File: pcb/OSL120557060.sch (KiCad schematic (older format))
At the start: 78 parts, among them J1 USB_B_Micro, J2 USB_B_Micro, J3 AVR-ISP-6, SW1 SW_SPST, SW10 SW_SPST, SW11 SW_SPST, SW12 SW_SPST, SW13 SW_SPST, SW14 SW_SPST, SW15 SW_SPST, SW16 SW_SPST, SW17 SW_SPST, SW18 SW_SPST, SW19 SW_SPST, SW2 SW_SPST, SW20 SW_SPST, SW21 SW_SPST, SW22 SW_SPST, SW23 SW_SPST, SW24 SW_SPST, SW25 SW_SPST, SW26 SW_SPST, SW27 SW_SPST, SW28 SW_SPST, SW29 SW_SPST, SW3 SW_SPST, SW30 SW_SPST, SW4 SW_SPST, SW5 SW_SPST, SW6 SW_SPST, SW7 SW_SPST, SW8 SW_SPST, SW9 SW_SPST, U1 ATmega328-PU, X1 16MHz

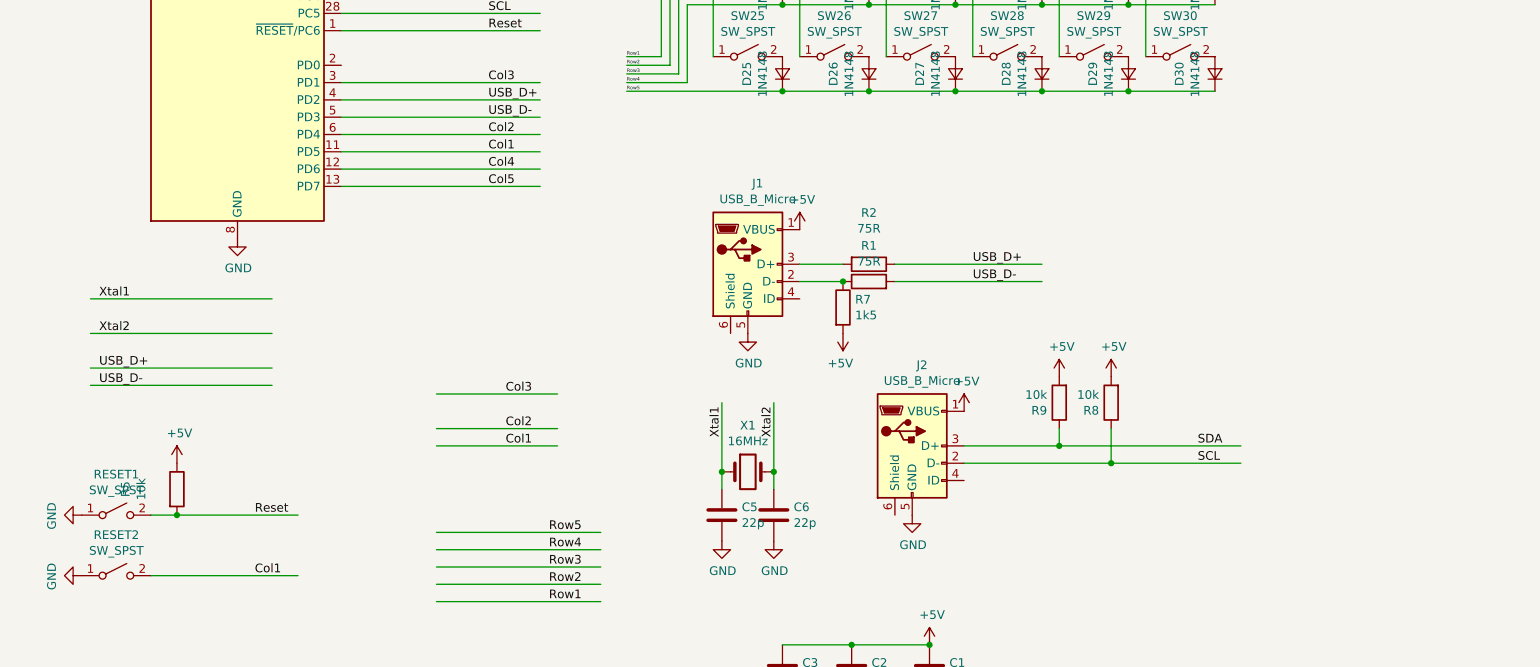
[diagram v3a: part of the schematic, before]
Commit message: * added missing zener diodes on the usb port
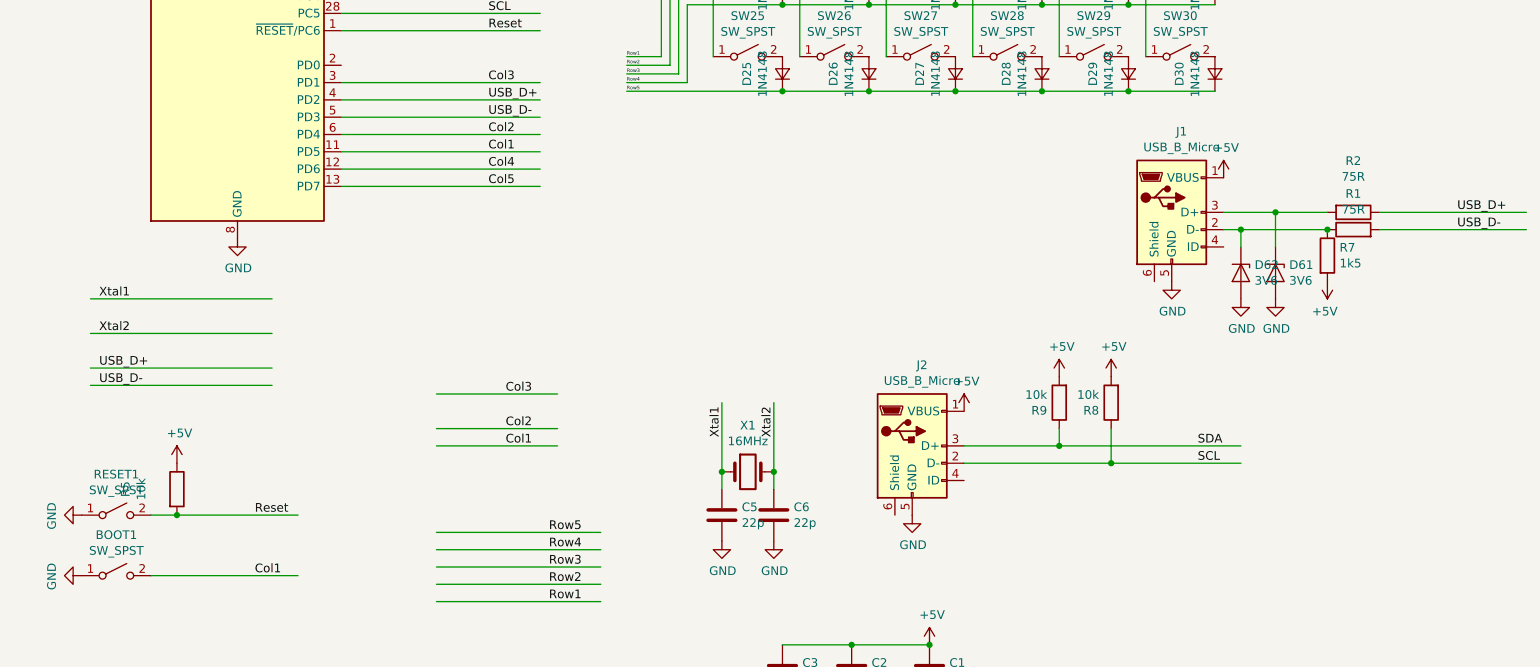
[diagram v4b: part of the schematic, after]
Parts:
- added D61, D62: 3V6, Diode_THT:D_T-1_P5.08mm_Horizontal, symbol Device:D_Zener
- renumbered RESET2 to BOOT1
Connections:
- wire segments 130 -> 134
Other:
- moved on the sheet: J1, R1, R2, R7
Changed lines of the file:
@@
 L power:+5V #PWR0107
 U 1 1 5D01457A
-P 5000 4500
-F 0 "#PWR0107" H 5000 4350 50  0001 C CNN
-F 1 "+5V" H 5015 4673 50  0000 C CNN
-F 2 "" H 5000 4500 50  0001 C CNN
-F 3 "" H 5000 4500 50  0001 C CNN
-	1    5000 4500
+P 7450 4200
+F 0 "#PWR0107" H 7450 4050 50  0001 C CNN
+F 1 "+5V" H 7465 4373 50  0000 C CNN
+F 2 "" H 7450 4200 50  0001 C CNN
+F 3 "" H 7450 4200 50  0001 C CNN
+	1    7450 4200
 	1    0    0    -1
 $EndComp
@@
 L power:GND #PWR0108
 U 1 1 5D014CE2
-P 4700 5100
-F 0 "#PWR0108" H 4700 4850 50  0001 C CNN
-F 1 "GND" H 4705 4927 50  0000 C CNN
-F 2 "" H 4700 5100 50  0001 C CNN
-F 3 "" H 4700 5100 50  0001 C CNN
-	1    4700 5100
+P 7150 4800
+F 0 "#PWR0108" H 7150 4550 50  0001 C CNN
+F 1 "GND" H 7155 4627 50  0000 C CNN
+F 2 "" H 7150 4800 50  0001 C CNN
+F 3 "" H 7150 4800 50  0001 C CNN
+	1    7150 4800
 	1    0    0    -1
 $EndComp
@@
 L Device:R R2
 U 1 1 5D015749
-P 5400 4700
-F 0 "R2" V 5103 4700 50  0000 C CNN
-F 1 "75R" V 5194 4700 50  0000 C CNN
-F 2 "Resistor_THT:R_Axial_DIN0207_L6.3mm_D2.5mm_P7.62mm_Horizontal" V 5285 4700 50  0001 C CNN
-F 3 "~" H 5400 4700 50  0001 C CNN
-	1    5400 4700
+P 8200 4400
+F 0 "R2" V 7903 4400 50  0000 C CNN
+F 1 "75R" V 7994 4400 50  0000 C CNN
+F 2 "Resistor_THT:R_Axial_DIN0207_L6.3mm_D2.5mm_P7.62mm_Horizontal" V 8085 4400 50  0001 C CNN
+F 3 "~" H 8200 4400 50  0001 C CNN
+	1    8200 4400
 	0    1    1    0
 $EndComp
@@
 L Device:R R1
 U 1 1 5D0160D0
-P 5400 4800
-F 0 "R1" V 5607 4800 50  0000 C CNN
-F 1 "75R" V 5516 4800 50  0000 C CNN
-F 2 "Resistor_THT:R_Axial_DIN0207_L6.3mm_D2.5mm_P7.62mm_Horizontal" V 5330 4800 50  0001 C CNN
-F 3 "~" H 5400 4800 50  0001 C CNN
-	1    5400 4800
-	0    -1   -1   0
-$EndComp
-Wire Wire Line
-	5000 4700 5250 4700
-Wire Wire Line
-	5550 4800 6400 4800
-Text Label 6000 4700 0    50   ~ 0
+P 8200 4500
+F 0 "R1" V 8407 4500 50  0000 C CNN
+F 1 "75R" V 8316 4500 50  0000 C CNN
+F 2 "Resistor_THT:R_Axial_DIN0207_L6.3mm_D2.5mm_P7.62mm_Horizontal" V 8130 4500 50  0001 C CNN
+F 3 "~" H 8200 4500 50  0001 C CNN
+	1    8200 4500
+	0    -1   -1   0
+$EndComp
+Wire Wire Line
+	8350 4500 9200 4500
+Text Label 8800 4400 0    50   ~ 0
 USB_D+
-Text Label 6000 4800 0    50   ~ 0
+Text Label 8800 4500 0    50   ~ 0
 USB_D-
 $Comp
@@
 	1    0    0    -1
 $EndComp
-Wire Wire Line
-	5000 4800 5250 4800
 $Comp
 L Device:R R7
 U 1 1 5D0E6210
-P 5250 4950
-F 0 "R7" H 5320 4996 50  0000 L CNN
-F 1 "1k5" H 5320 4905 50  0000 L CNN
-F 2 "Resistor_THT:R_Axial_DIN0207_L6.3mm_D2.5mm_P7.62mm_Horizontal" V 5180 4950 50  0001 C CNN
-F 3 "~" H 5250 4950 50  0001 C CNN
-	1    5250 4950
-	1    0    0    -1
-$EndComp
-Connection ~ 5250 4800
+P 8050 4650
+F 0 "R7" H 8120 4696 50  0000 L CNN
+F 1 "1k5" H 8120 4605 50  0000 L CNN
+F 2 "Resistor_THT:R_Axial_DIN0207_L6.3mm_D2.5mm_P7.62mm_Horizontal" V 7980 4650 50  0001 C CNN
+F 3 "~" H 8050 4650 50  0001 C CNN
+	1    8050 4650
+	1    0    0    -1
+$EndComp
+Connection ~ 8050 4500
 $Comp
 L power:+5V #PWR0116
 U 1 1 5D0E723C
-P 5250 5100
-F 0 "#PWR0116" H 5250 4950 50  0001 C CNN
-F 1 "+5V" H 5265 5273 50  0000 C CNN
-F 2 "" H 5250 5100 50  0001 C CNN
-F 3 "" H 5250 5100 50  0001 C CNN
-	1    5250 5100
+P 8050 4800
+F 0 "#PWR0116" H 8050 4650 50  0001 C CNN
+F 1 "+5V" H 8065 4973 50  0000 C CNN
+F 2 "" H 8050 4800 50  0001 C CNN
+F 3 "" H 8050 4800 50  0001 C CNN
+	1    8050 4800
 	-1   0    0    1
 $EndComp
@@
 L Connector:USB_B_Micro J1
 U 1 1 5CFFA047
-P 4700 4700
-F 0 "J1" H 4757 5167 50  0000 C CNN
-F 1 "USB_B_Micro" H 4757 5076 50  0000 C CNN
-F 2 "Connector_USB:USB_Micro-B_Molex-105017-0001" H 4850 4650 50  0001 C CNN
-F 3 "~" H 4850 4650 50  0001 C CNN
-	1    4700 4700
+P 7150 4400
+F 0 "J1" H 7207 4867 50  0000 C CNN
+F 1 "USB_B_Micro" H 7207 4776 50  0000 C CNN
+F 2 "Connector_USB:USB_Micro-B_Molex-105017-0001" H 7300 4350 50  0001 C CNN
+F 3 "~" H 7300 4350 50  0001 C CNN
+	1    7150 4400
 	1    0    0    -1
 $EndComp
@@
 	6500 5750 7550 5750
 $Comp
-L Switch:SW_SPST RESET2
+L Switch:SW_SPST BOOT1
 U 1 1 5D1219A3
 P 1050 6500
-F 0 "RESET2" H 1050 6735 50  0000 C CNN
+F 0 "BOOT1" H 1050 6735 50  0000 C CNN
 F 1 "SW_SPST" H 1050 6644 50  0000 C CNN
 F 2 "Button_Switch_SMD:SW_SPST_B3U-1000P" H 1050 6500 50  0001 C CNN
@@
 Col1
 Wire Wire Line
-	5550 4700 6400 4700
+	8350 4400 9200 4400
+$Comp
+L Device:D_Zener D62
+U 1 1 5D157151
+P 7550 4750
+F 0 "D62" V 7504 4829 50  0000 L CNN
+F 1 "3V6" V 7595 4829 50  0000 L CNN
+F 2 "Diode_THT:D_T-1_P5.08mm_Horizontal" H 7550 4750 50  0001 C CNN
+F 3 "~" H 7550 4750 50  0001 C CNN
+	1    7550 4750
+	0    1    1    0
+$EndComp
+$Comp
+L Device:D_Zener D61
+U 1 1 5D1584AC
+P 7750 4750
+F 0 "D61" V 7704 4829 50  0000 L CNN
+F 1 "3V6" V 7795 4829 50  0000 L CNN
+F 2 "Diode_THT:D_T-1_P5.08mm_Horizontal" H 7750 4750 50  0001 C CNN
+F 3 "~" H 7750 4750 50  0001 C CNN
+	1    7750 4750
+	0    1    1    0
+$EndComp
+$Comp
+L power:GND #PWR0120
+U 1 1 5D159131
+P 7550 4900
+F 0 "#PWR0120" H 7550 4650 50  0001 C CNN
+F 1 "GND" H 7555 4727 50  0000 C CNN
+F 2 "" H 7550 4900 50  0001 C CNN
+F 3 "" H 7550 4900 50  0001 C CNN
+	1    7550 4900
+	1    0    0    -1
+$EndComp
+$Comp
+L power:GND #PWR0121
+U 1 1 5D15E973
+P 7750 4900
+F 0 "#PWR0121" H 7750 4650 50  0001 C CNN
+F 1 "GND" H 7755 4727 50  0000 C CNN
+F 2 "" H 7750 4900 50  0001 C CNN
+F 3 "" H 7750 4900 50  0001 C CNN
+	1    7750 4900
+	1    0    0    -1
+$EndComp
+Wire Wire Line
+	7450 4500 7550 4500
+Wire Wire Line
+	7450 4400 7750 4400
+Wire Wire Line
+	7750 4600 7750 4400
+Connection ~ 7750 4400
+Wire Wire Line
+	7750 4400 8050 4400
+Wire Wire Line
+	7550 4600 7550 4500
+Connection ~ 7550 4500
+Wire Wire Line
+	7550 4500 8050 4500
 $EndSCHEMATC

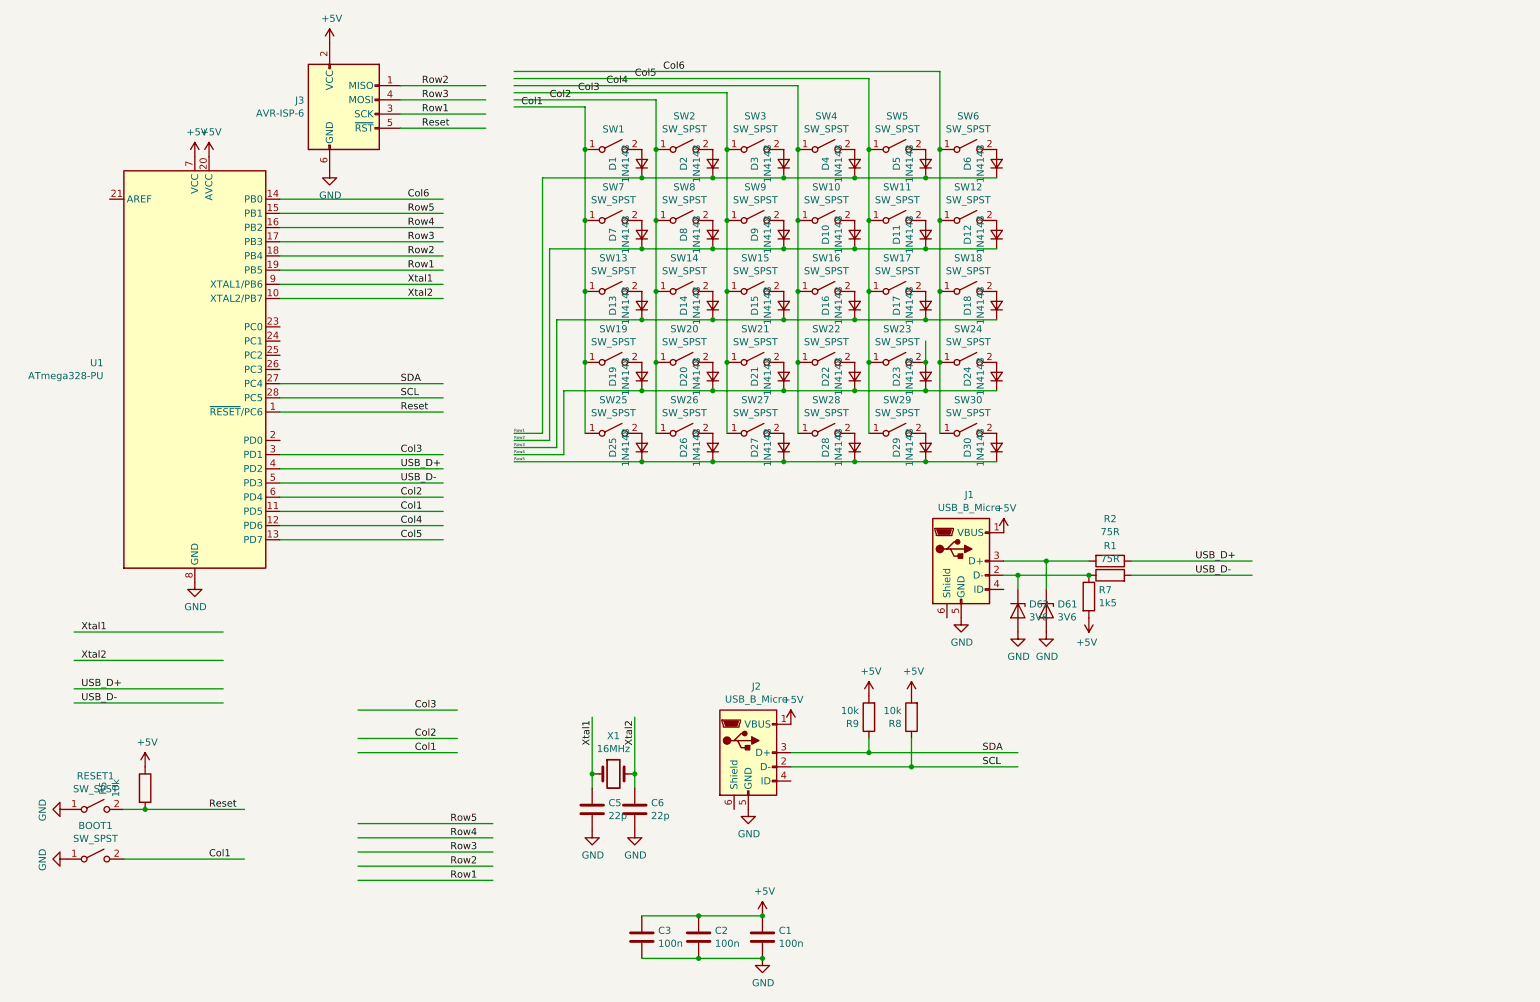
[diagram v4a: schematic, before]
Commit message: moved from micro usb to usb-c (yw wilba)
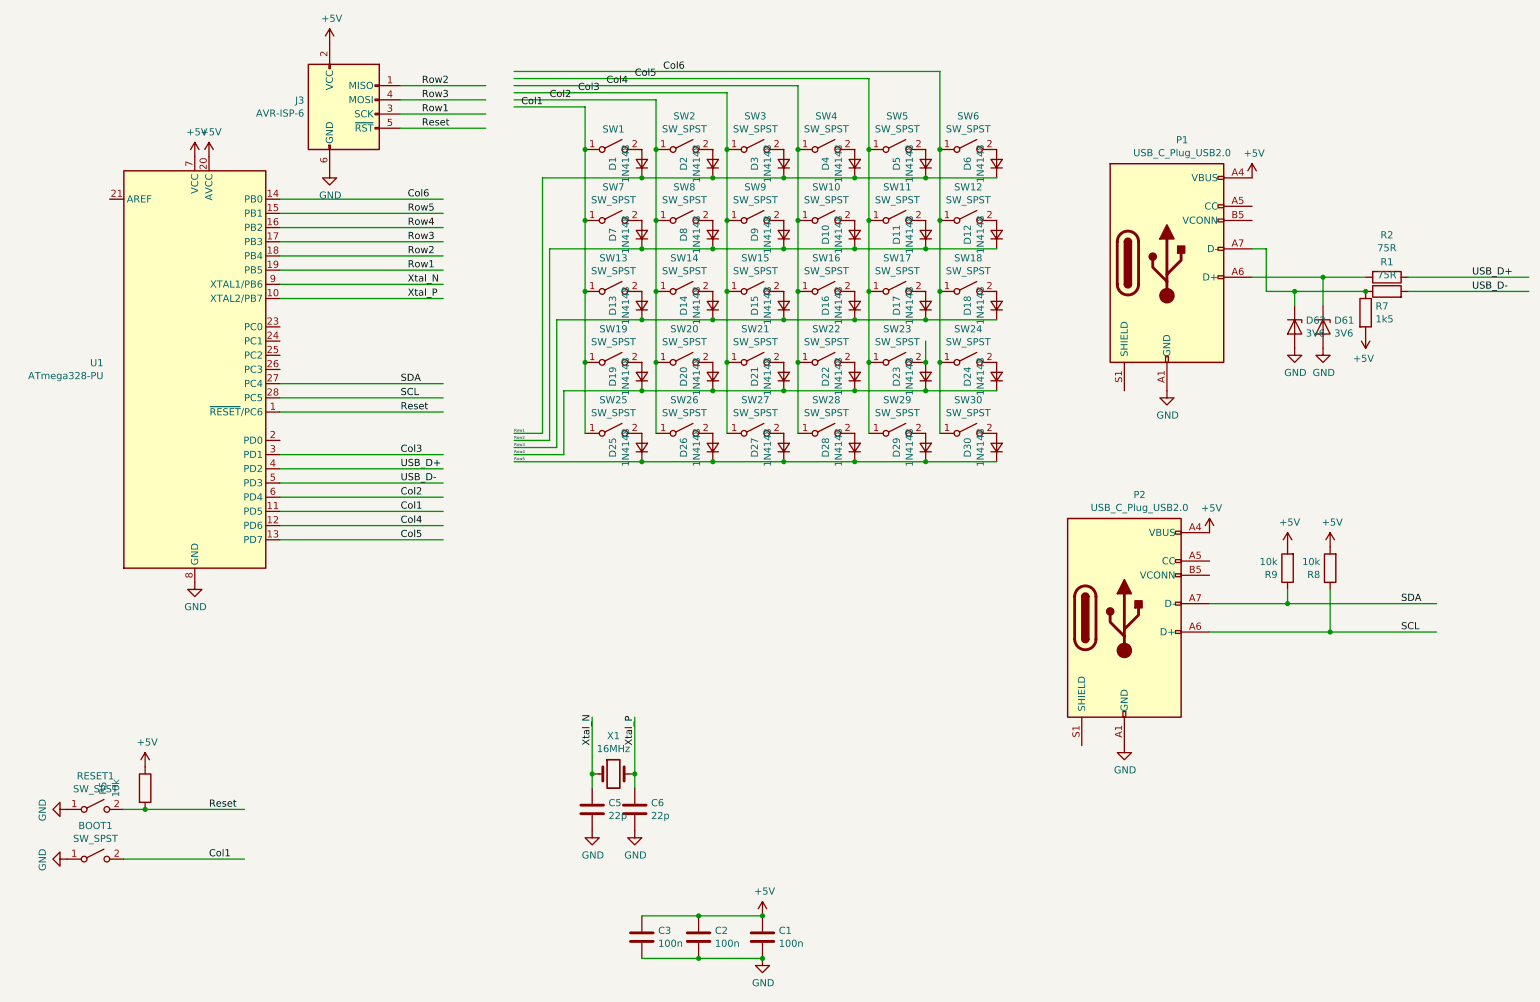
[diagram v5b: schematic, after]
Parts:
- removed J1, J2: USB_B_Micro, Connector_USB:USB_Micro-B_Molex-105017-0001, symbol Connector:USB_B_Micro
- added P1, P2: USB_C_Plug_USB2.0, Connector_USB:USB_C_Receptacle_GCT_USB4085, symbol Connector:USB_C_Plug_USB2.0
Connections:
- net labels added: Xtal_N, Xtal_P
- net labels removed: Xtal1, Xtal2
- wire segments 134 -> 124
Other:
- moved on the sheet: D61, D62, R1, R2, R7, R8, R9

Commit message: * added mount pis to pcb * improved plate layout
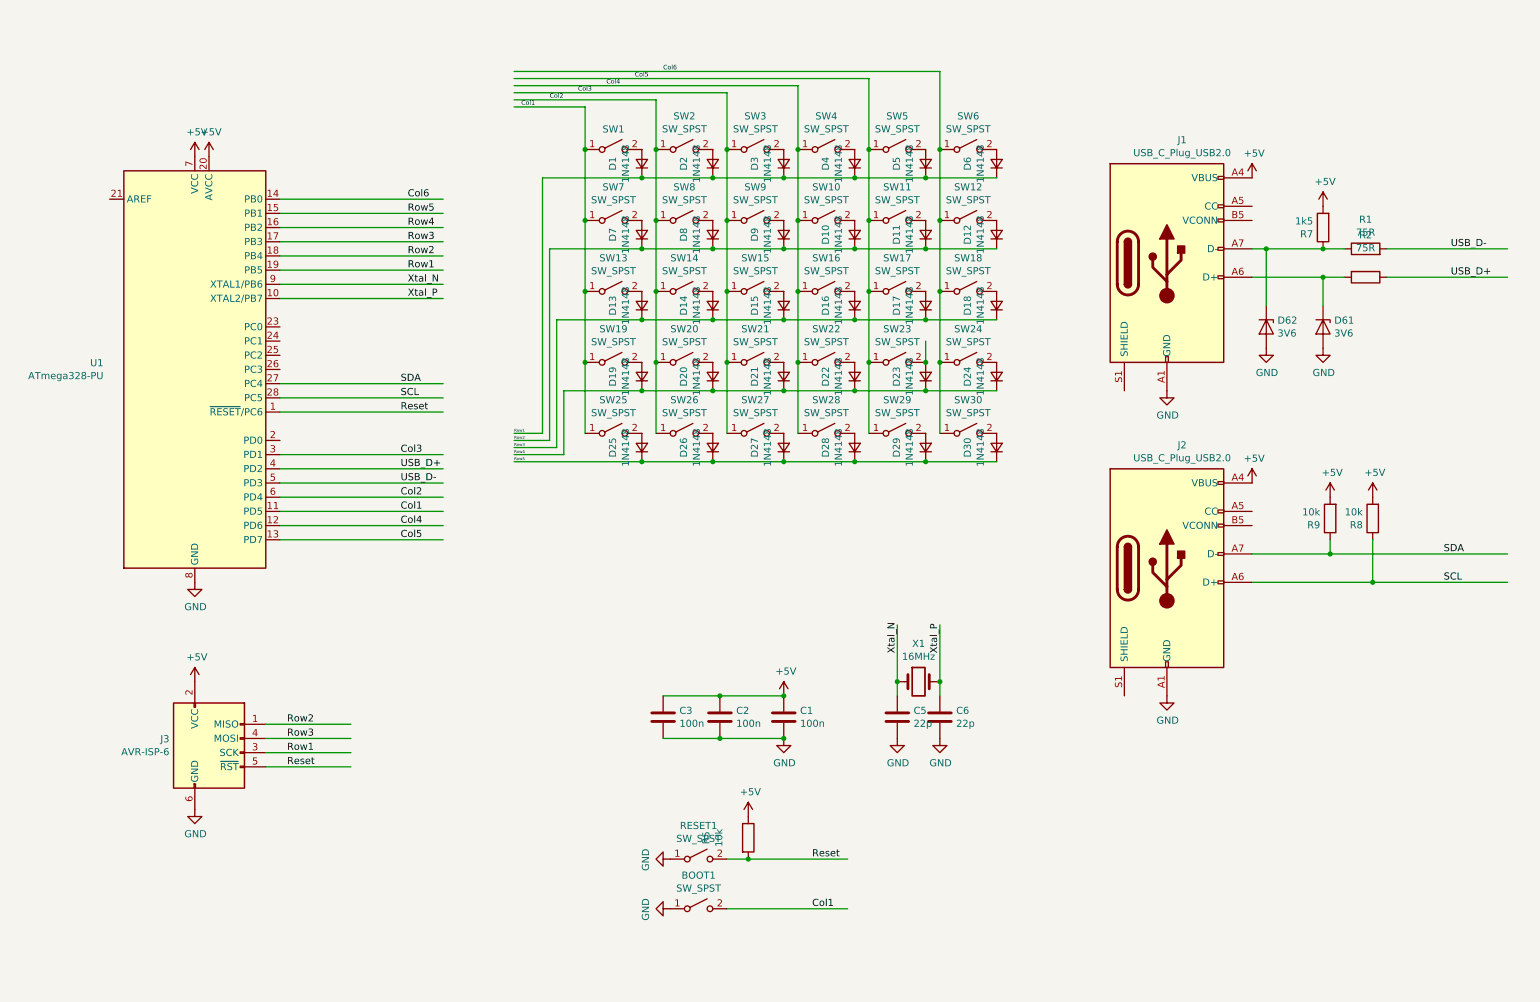
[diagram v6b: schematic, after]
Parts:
- renumbered P1 to J1, P2 to J2
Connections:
- wire segments 124 -> 123
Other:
- moved on the sheet: BOOT1, C1, C2, C3, C5, C6, D62, J2, J3, R1, R2, R5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
